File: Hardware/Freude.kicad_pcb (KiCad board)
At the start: 4 copper layers, 65.3 x 26.4 mm, 39 parts, among them J1 Conn_01x06_Female, J10 Conn_01x06_Female, J11 Conn_01x05_Male, J12 Conn_01x05_Female, J2 Conn_01x05_Female, J3 Conn_01x06_Female, J4 Conn_01x04_Female, J5 Conn_01x04_Female, J6 Conn_01x04_Male, J7 Conn_01x03_Female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

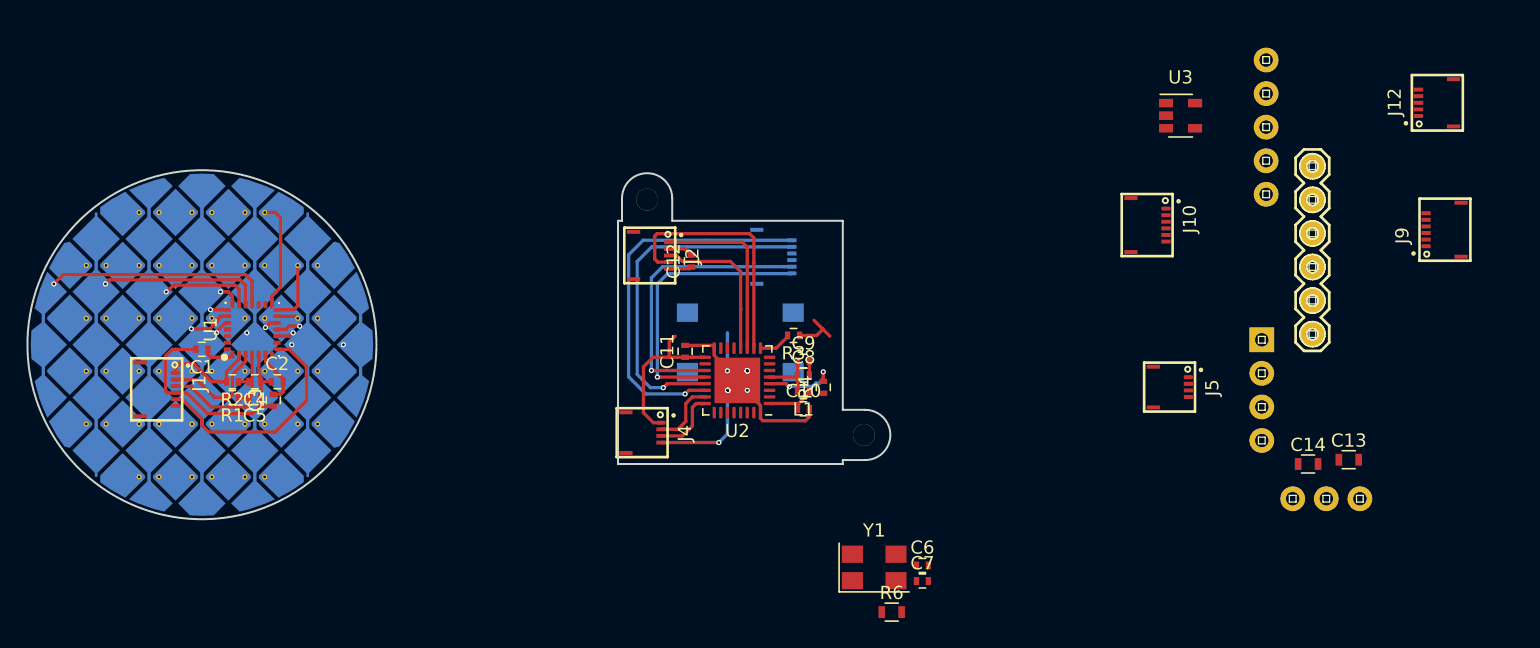
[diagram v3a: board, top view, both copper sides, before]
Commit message: add led, change sw1 footprint, add testpads
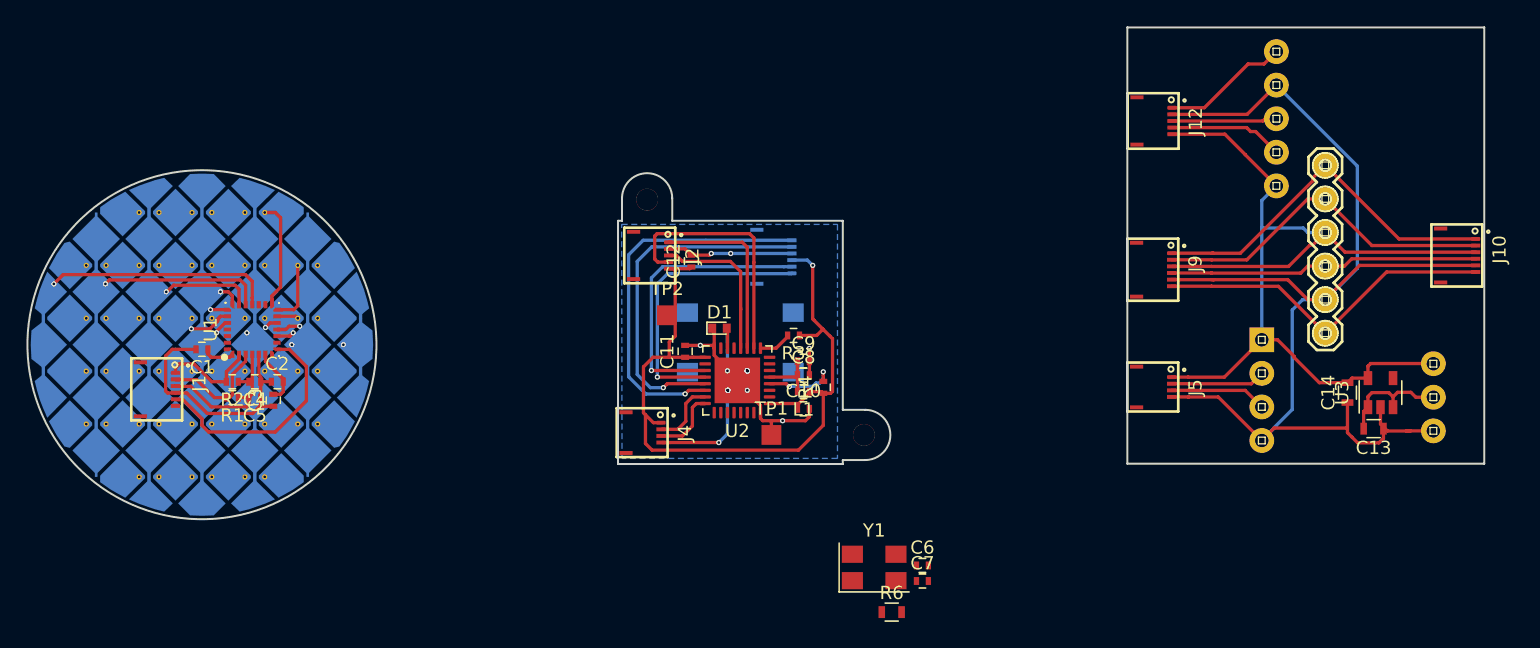
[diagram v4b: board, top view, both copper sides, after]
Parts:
- removed the REF** at (200.7, 79.8)
- added D1: 16-213/GHC-YR1S1/3T, LEDs:LED_0402, F.Cu at (199.2, 78.8)
- added SW1: B3FS-1015P`, .pretty:B3FS-1015P, B.Cu at (200.7, 79.8)
- added TP1: TestPoint, Measurement_Points:Measurement_Point_Square-SMD-Pad_Small, F.Cu at (203.1, 86.8)
- added TP2: TestPoint, Measurement_Points:Measurement_Point_Square-SMD-Pad_Small, F.Cu at (195.2, 77.8)
- moved U3 25.8 mm to (249.2, 83.6), turned to 90 degrees
- moved J10 23.5 mm to (256.4, 73.2)
- moved J9 19.5 mm to (233.3, 74.3), turned to 270 degrees
- moved J12 18.7 mm to (233.4, 63.1), turned to 270 degrees
- moved J8 12.8 mm to (245.0, 66.4), turned to 270 degrees
- moved J7 11.6 mm to (253.2, 81.4), turned to 270 degrees
- moved J11 10.8 mm to (241.3, 57.8), turned to 270 degrees
- moved C14 6.17 mm to (246.7, 83.6), turned to 90 degrees
- moved C13 3.01 mm to (248.6, 86.3), turned to 180 degrees
- moved J5 1.27 mm to (233.3, 83.2)
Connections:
- J11 pad 4: /DAC2_OUT1_BO -> /DAC1_OUT2_BO
- J12 pad 4: /DAC2_OUT1_BO -> /DAC1_OUT2_BO
- J7 pad 1: VCC -> +1V8
- J7 pad 2: +1V8 -> VCC
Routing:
- net GNDA: track 19.1 -> 113.6 mm
- net +1V8: track 0.00 -> 75.0 mm
- net +3V3: track 21.3 -> 57.5 mm, vias 0 -> 1
- net /SDA_BO: track 0.00 -> 28.4 mm
- net /UNK_BO: track 0.00 -> 26.4 mm
- net /SCL_BO: track 0.00 -> 26.4 mm
- net /RDY_BO: track 0.00 -> 23.5 mm
- net GND: track 29.5 -> 40.9 mm, vias 11 -> 16
- net /DAC2_OUT1_BO: track 0.00 -> 9.86 mm
- net /DAC1_OUT2_BO: track 0.00 -> 8.87 mm
- net VCC: track 0.00 -> 8.84 mm
- net /Switch_Out_BO: track 0.00 -> 8.17 mm
- net /Prog_SWCLK: track 0.00 -> 7.34 mm
- net /Prog_SWDIO: track 0.00 -> 7.15 mm
- net Net-(D1-Pad2): track 0.00 -> 1.61 mm
- added copper zone on B.Cu, net GND
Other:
- board size 65.3 x 26.4 mm -> 110.2 x 37.2 mm

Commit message: rearrange and rerout
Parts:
- added C15: 100pF, Resistors_SMD:R_0402, F.Cu at (202.1, 79.1)
- R6: footprint Resistors_SMD:R_0603 -> Resistors_SMD:R_0402
- moved C7 18.8 mm to (217.0, 79.2)
- moved R6 17.7 mm to (214.3, 82.6), turned to 90 degrees
- moved Y1 15.4 mm to (217.0, 82.7), turned to 90 degrees
- moved J3 12.5 mm to (200.7, 85.2), turned to 180 degrees
- moved C6 10.7 mm to (216.9, 86.2)
- moved L1 4.28 mm to (205.6, 79.3)
- moved R4 3.91 mm to (207.3, 79.3)
- moved C10 1.77 mm to (203.8, 85.4), turned to 270 degrees
- moved C8 1.18 mm to (204.7, 81.5)
- moved C9 1.18 mm to (204.7, 80.4)
- moved C11 0.85 mm to (195.7, 80.5)
- moved TP2 0.85 mm to (194.3, 77.8)
- moved D1 0.85 mm to (198.3, 78.7)
- moved TP1 0.85 mm to (202.2, 86.8)
- moved U2 0.85 mm to (199.7, 82.7)
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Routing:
- net +3V3: track 57.5 -> 35.4 mm, vias 1 -> 0
- net /Switch_In: track 2.51 -> 13.6 mm, vias 0 -> 1
- net GND: track 40.9 -> 44.2 mm
- net Net-(C8-Pad1): track 4.47 -> 2.17 mm
- net Net-(R4-Pad2): track 5.68 -> 4.96 mm, vias 2 -> 1

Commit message: rerouted, tidied
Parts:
- moved R6 11.2 mm to (203.1, 83.7), turned to 0 degrees
- moved Y1 10.8 mm to (206.2, 83.8)
- moved C6 10.8 mm to (206.2, 87.3)
- moved C7 10.6 mm to (206.5, 80.4)
- moved R4 2.71 mm to (204.8, 80.4), turned to 180 degrees
- moved C8 1.53 mm to (203.1, 81.5)
- moved C9 1.53 mm to (203.1, 80.4)
- moved C10 0.98 mm to (202.9, 85.9)
- moved C15 0.80 mm to (201.2, 79.1)
- moved D1 0.80 mm to (197.5, 78.7)
- moved L1 0.80 mm to (204.8, 79.3)
- moved U2 0.80 mm to (198.8, 82.7)
- moved C11 0.80 mm to (194.9, 80.5)
- moved TP1 0.80 mm to (201.4, 86.8)
- moved TP2 0.80 mm to (193.5, 77.8)
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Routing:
- net /AZO_UNK: track 28.5 -> 7.52 mm
- net /RDY_UC: track 26.4 -> 9.18 mm
- net +3V3: track 35.4 -> 52.6 mm, vias 0 -> 4
- net /SDA_UC: track 21.2 -> 9.42 mm
- net /SCL_UC: track 22.0 -> 11.3 mm
- net Net-(C6-Pad2): track 0.00 -> 8.88 mm
- net Net-(C7-Pad1): track 0.00 -> 5.14 mm
- net Net-(C8-Pad1): track 2.17 -> 5.51 mm
- net GND: track 44.2 -> 47.2 mm, vias 16 -> 13
- net /DAC2_OUT1: track 13.7 -> 11.9 mm
- net /DAC1_OUT2: track 18.9 -> 17.1 mm
- net /SWCLK: track 5.46 -> 3.71 mm
- net /Switch_In: track 13.6 -> 15.4 mm, vias 1 -> 2
- net /Switch_Out: track 11.9 -> 10.3 mm
- net Net-(R6-Pad1): track 0.00 -> 1.48 mm
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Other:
- net class Default: clearance 0.018 -> 0.1
- rule trace_clearance: 0.018 -> 0.1

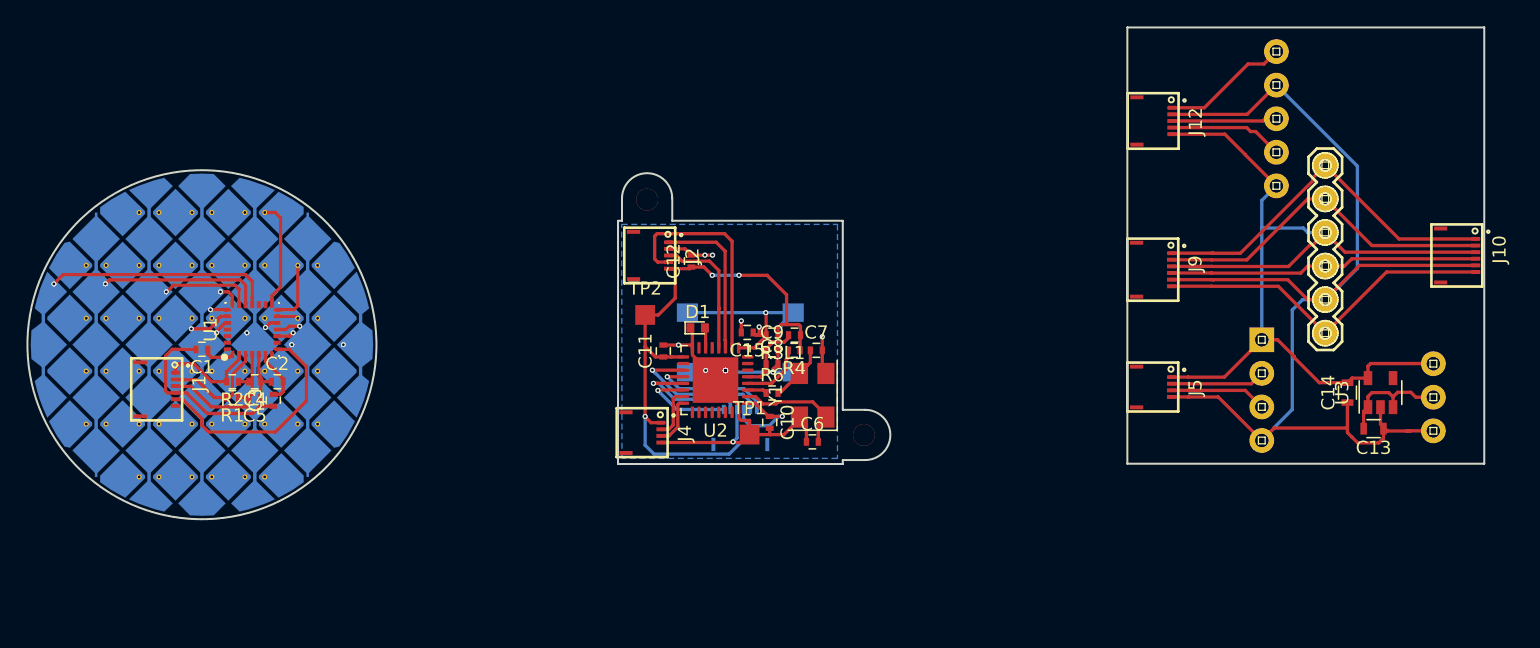
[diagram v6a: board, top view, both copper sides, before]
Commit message: routing on boards finished. Will change to 3 board projects for 3d reasons. Considering branch
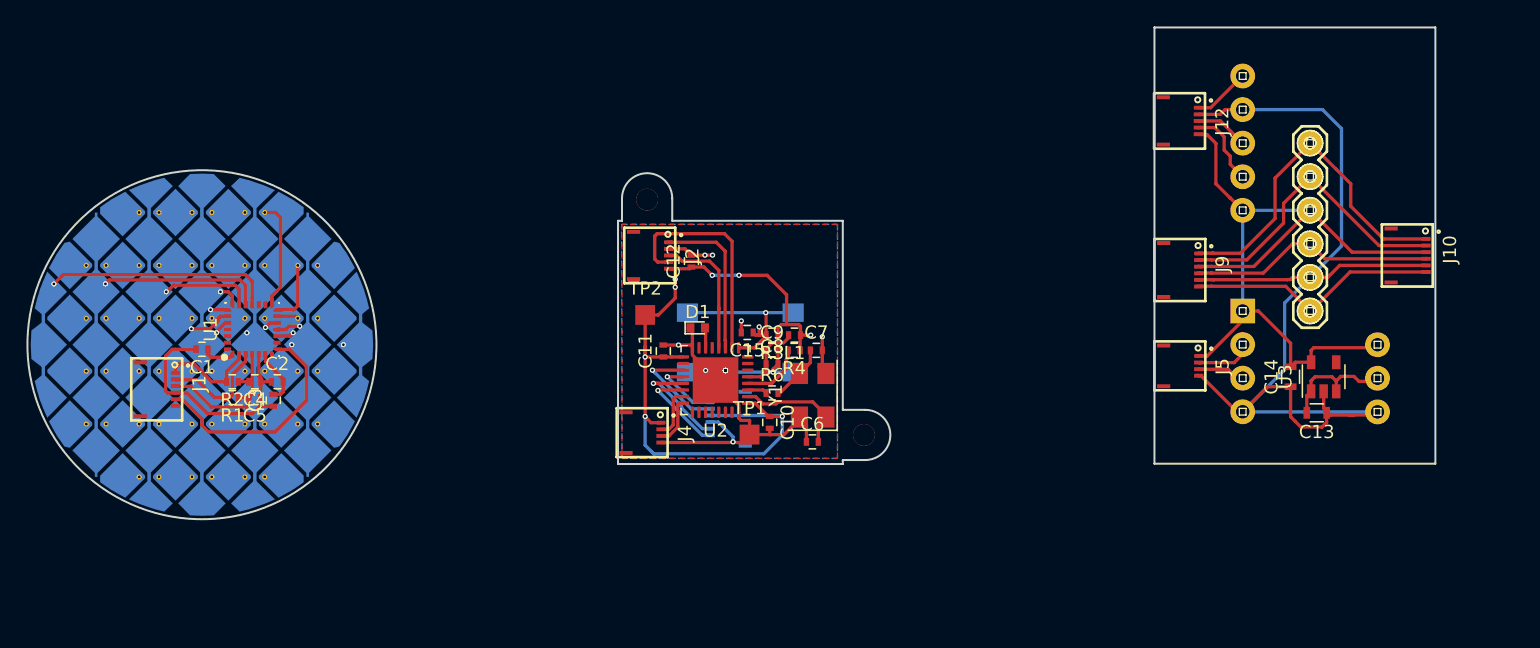
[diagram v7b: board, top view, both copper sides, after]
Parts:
- moved C14 4.46 mm to (242.3, 82.4)
- moved U3 4.46 mm to (244.8, 82.4)
- moved C13 4.46 mm to (244.3, 85.2)
- moved J7 4.46 mm to (248.9, 80.0)
- moved J10 3.75 mm to (252.6, 73.2)
- moved J11 3.15 mm to (238.7, 59.7)
- moved J6 2.61 mm to (238.7, 77.5)
- moved J5 2.60 mm to (235.4, 81.6)
- moved J3 2.38 mm to (198.4, 85.6), turned to 270 degrees
- moved J9 2.05 mm to (235.4, 74.3)
- moved J8 2.04 mm to (243.8, 64.8)
- moved J12 2.00 mm to (235.4, 63.1)
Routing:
- net +1V8: track 75.0 -> 59.3 mm
- net GNDA: track 113.6 -> 105.5 mm
- net /UNK_BO: track 26.4 -> 19.4 mm
- net +3V3: track 52.6 -> 58.8 mm, vias 4 -> 8
- net /DAC2_OUT1_BO: track 9.86 -> 4.91 mm
- net /RDY_BO: track 23.5 -> 18.9 mm
- net /SDA_UC: track 9.42 -> 5.32 mm
- net /Switch_Out_BO: track 8.17 -> 4.08 mm
- net /SCL_BO: track 26.4 -> 23.0 mm
- net /SCL_UC: track 11.3 -> 7.92 mm
- net /Prog_SWDIO: track 7.15 -> 3.77 mm
- net /Prog_SWCLK: track 7.34 -> 3.99 mm
- net /DAC1_OUT2_BO: track 8.87 -> 5.88 mm
- net /SDA_BO: track 28.4 -> 26.6 mm
- net /Switch_In: track 15.4 -> 13.9 mm
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- added copper zone on F.Cu, net +3V3
- added copper zone on In1.Cu, net +3V3
- added copper zone on In2.Cu, net GND
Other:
- board size 110.2 x 37.2 mm -> 106.5 x 37.2 mm
